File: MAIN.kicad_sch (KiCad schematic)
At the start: 47 parts, among them J2 Conn_01x02_Socket, J3 Conn_01x03, J6 USB_C_Receptacle_USB2.0_16P, SW1 SW_Push, SW2 SW_Push, SW3 SW_Push, SW4 SW_Push, SW5 SW_Push, U1 USBLC6-2SC6, U2 ESP32-S3-MINI-1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

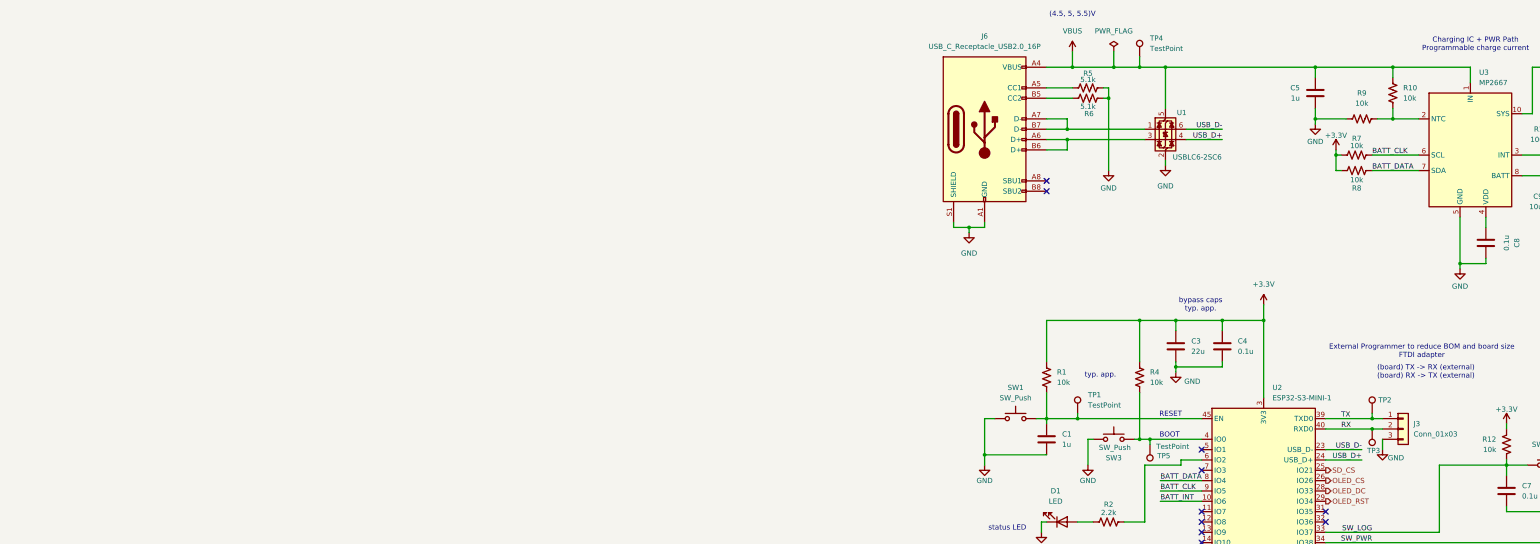
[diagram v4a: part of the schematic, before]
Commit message: modified BOM
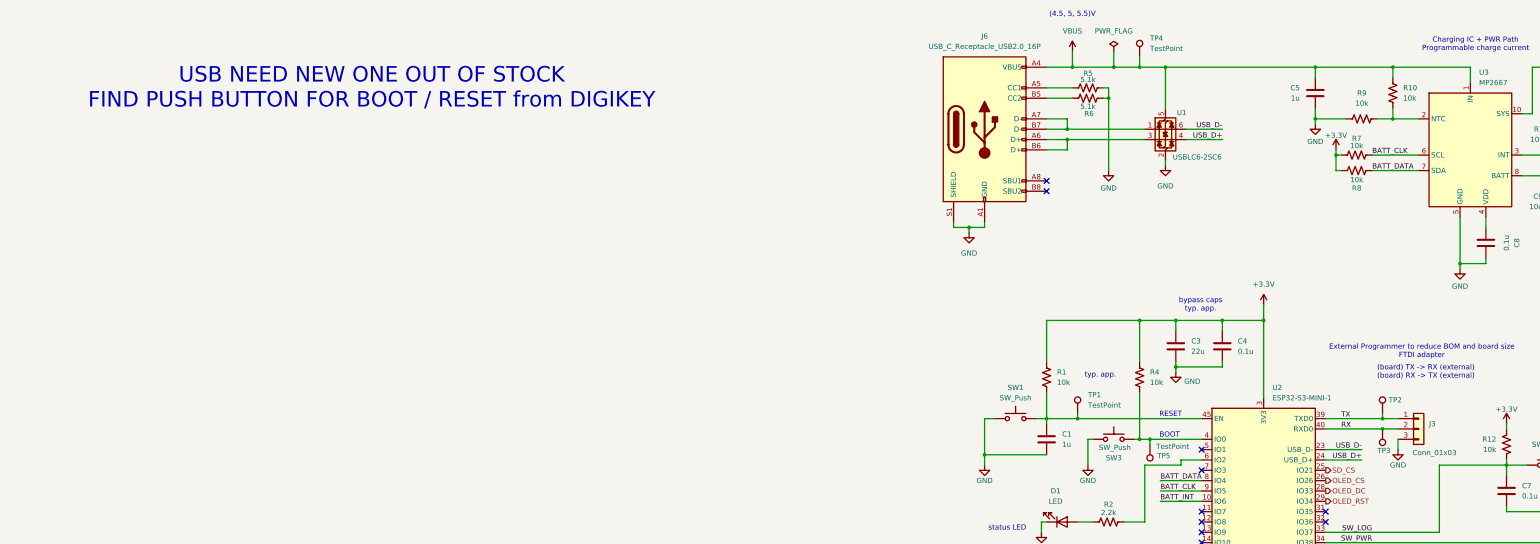
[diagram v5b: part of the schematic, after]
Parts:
- C1, C5: Distributor Link https://www.lcsc.com/product-detail/C24123.html -> https://www.digikey.com/en/products/detail/samsung-electro-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; MPN CL21B105KOFNNNE -> CL21B105KOFNNWE
- C10: Distributor Link https://www.lcsc.com/product-detail/C28234.html -> https://www.digikey.com/en/products/detail/samsung-electro-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
- C11, C12, C9: Distributor Link https://www.lcsc.com/product-detail/C95841.html -> https://www.digikey.com/en/products/detail/samsung-electro-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
- C2, C4, C6, C7, C8: Distributor Link https://www.lcsc.com/product-detail/C519980.html -> https://www.digikey.com/en/products/detail/samsung-electro-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; MPN CC0805KRX7R7BB104 -> CL21B104KBCNNNC; Manufacturer YAGEO -> Samsung Electro-Mechanics
- C3: Distributor Link https://www.lcsc.com/product-detail/C98190.html -> https://www.digikey.com/en/products/detail/samsung-electro-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; MPN CL21A226MOQNNNE -> CL21A226MOCLRNC
- D1: Distributor Link https://www.lcsc.com/product-detail/C965812.html -> https://www.digikey.com/en/products/detail/liteon/LTST-C170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; MPN XL-2012SURC -> LTST-C170GKT; Manufacturer XINGLIGHT -> Lite-On Inc.
- R1, R10, R11, R12, R3, R4, R7, R8, R9: Distributor Link https://www.lcsc.com/product-detail/C17414.html -> https://www.digikey.com/en/products/detail/yageo/RC0805JR-0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; MPN 0805W8F1002T5E -> RC0805JR-0710KL; Manufacturer UNI-ROYAL -> YAGEO
- R13: Distributor Link https://www.lcsc.com/product-detail/C149504.html -> https://www.digikey.com/en/products/detail/yageo/RC0805FR-0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; MPN 0805W8F1003T5E -> RC0805FR-07100KL; Manufacturer UNI-ROYAL -> YAGEO
- R2: Distributor Link https://www.lcsc.com/product-detail/C17520.html -> https://www.digikey.com/en/products/detail/yageo/RC0805FR-0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; MPN 0805W8F2201T5E -> RC0805FR-072K2L; Manufacturer UNI-ROYAL -> YAGEO
- R5, R6: Distributor Link https://www.lcsc.com/product-detail/C27834.html -> https://www.digikey.com/en/products/detail/yageo/RC0805JR-0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; MPN 0805W8F5101T5E -> RC0805JR-075K1L; Manufacturer UNI-ROYAL -> YAGEO
- U1: Distributor Link https://www.lcsc.com/product-detail/C2827654.html?s_z=n_USB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 -> https://www.digikey.com/en/products/detail/stmicroelectroni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; Manufacturer TECH PUBLIC -> STMicroelectronics
- U2: Distributor Link https://www.lcsc.com/product-detail/C2913206.html?s_z=n_esp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 -> https://www.digikey.com/en/products/detail/espressif-system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; Manufacturer ESPRESSIF -> Espressif Systems
- U4: Distributor Link https://www.lcsc.com/product-detail/C86534.html?s_z=n_xc622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 -> https://www.digikey.com/en/products/detail/torex-semiconduc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; Manufacturer TOREX -> Torex Semiconductor Ltd
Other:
- note added: "USB NEED NEW ONE OUT OF STOCK FIND PUSH BUTTON FOR BOOT / RESET from DIGIKEY"
- moved on the sheet: J3, TP2, TP3

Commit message: new push button
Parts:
- J6: Distributor Link https://www.digikey.com/en/products/detail/gct/USB4105-GF-A/11198441 -> https://www.digikey.com/en/products/detail/gct/USB4105-GF-A-120/14559037
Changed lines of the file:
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@@
 			)
 		)
-		(property "Distributor Link" "https://www.digikey.com/en/products/detail/gct/USB4105-GF-A/11198441"
+		(property "Distributor Link" "https://www.digikey.com/en/products/detail/gct/USB4105-GF-A-120/14559037"
 			(at 39.37 45.72 0)
 			(effects

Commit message: modified layout
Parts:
- SW1, SW3: footprint Button_Switch_SMD:SW_SPST_TS-1088-xR020 -> Button_Switch_SMD:SW_SPST_B3U-1000P; Distributor Link https://www.lcsc.com/product-detail/C720477.html?s_z=n_push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 -> https://www.digikey.com/en/products/detail/omron-electronic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; MPN TS-1088-AR02016 -> B3U-1000P; Manufacturer XUNPU -> Omron Electronics Inc-EMC Div
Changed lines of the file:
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@@
 			)
 		)
-		(property "Footprint" "Button_Switch_SMD:SW_SPST_TS-1088-xR020"
+		(property "Footprint" "Button_Switch_SMD:SW_SPST_B3U-1000P"
 			(at 71.12 116.84 0)
 			(effects
@@
 			)
 		)
-		(property "Datasheet" "https://www.lcsc.com/datasheet/C720477.pdf"
+		(property "Datasheet" ""
 			(at 71.12 116.84 0)
 			(effects
@@
 			)
 		)
-		(property "MPN" "TS-1088-AR02016"
+		(property "MPN" "B3U-1000P"
 			(at 71.12 121.92 0)
 			(effects
@@
 			)
 		)
-		(property "Manufacturer" "XUNPU"
+		(property "Manufacturer" "Omron Electronics Inc-EMC Div"
 			(at 71.12 121.92 0)
 			(effects
@@
 			)
 		)
-		(property "Distributor Link" "https://www.lcsc.com/product-detail/C720477.html?s_z=n_push%2520button%2520switch"
+		(property "Distributor Link" "https://www.digikey.com/en/products/detail/omron-electronics-inc-emc-div/B3U-1000P/1534338?gclsrc=aw.ds&gad_source=1&gad_campaignid=120565755&gbraid=0AAAAADrbLlg0O0xjmCmUbyKlcuGb4oGh0&gclid=CjwKCAiA4KfLBhB0EiwAUY7GAQ-b3iPcxPGC034MJCcv0szfw6wekoSPvS7JzjO8BYSXgQE8oVGvMRoCSdUQAvD_BwE"
 			(at 71.12 121.92 0)
 			(effects
@@
 			)
 		)
-		(property "Footprint" "Button_Switch_SMD:SW_SPST_TS-1088-xR020"
+		(property "Footprint" "Button_Switch_SMD:SW_SPST_B3U-1000P"
 			(at 46.99 111.76 0)
 			(effects
@@
 			)
 		)
-		(property "Datasheet" "https://www.lcsc.com/datasheet/C720477.pdf"
+		(property "Datasheet" ""
 			(at 46.99 111.76 0)
 			(effects
@@
 			)
 		)
-		(property "MPN" "TS-1088-AR02016"
+		(property "MPN" "B3U-1000P"
 			(at 46.99 116.84 0)
 			(effects
@@
 			)
 		)
-		(property "Manufacturer" "XUNPU"
+		(property "Manufacturer" "Omron Electronics Inc-EMC Div"
 			(at 46.99 116.84 0)
 			(effects
@@
 			)
 		)
-		(property "Distributor Link" "https://www.lcsc.com/product-detail/C720477.html?s_z=n_push%2520button%2520switch"
+		(property "Distributor Link" "https://www.digikey.com/en/products/detail/omron-electronics-inc-emc-div/B3U-1000P/1534338?gclsrc=aw.ds&gad_source=1&gad_campaignid=120565755&gbraid=0AAAAADrbLlg0O0xjmCmUbyKlcuGb4oGh0&gclid=CjwKCAiA4KfLBhB0EiwAUY7GAQ-b3iPcxPGC034MJCcv0szfw6wekoSPvS7JzjO8BYSXgQE8oVGvMRoCSdUQAvD_BwE"
 			(at 46.99 116.84 0)
 			(effects

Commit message: modified battery terminal
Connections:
- net +BATT: now also J2.1 (Pin_1); no longer J2.2 (Pin_2)
- net GND: now also J2.2 (Pin_2); no longer J2.1 (Pin_1)
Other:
- note removed: "External Programmer to reduce BOM and board size FTDI adapter"
- note removed: "USB NEED NEW ONE OUT OF STOCK FIND PUSH BUTTON FOR BOOT / RESET from DIGIKEY"
- moved on the sheet: C1, C2, C3, C4, C6, C7, D1, J3, R1, R11, R12, R2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
